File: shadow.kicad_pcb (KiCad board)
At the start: 2 copper layers, 25 parts, among them IC1 FS312F-G, J1 USB_C_Receptacle, Q1 FS8205, SW1 SW_Push, SW2 SW_Push, SW3 SW_SPST, U1 Arduino Nano 33 IoT, U8 TP4056, U9 MT3608

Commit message: start work on pcb design
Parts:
- added C5: 10uf, Capacitor_SMD:C_0201_0603Metric, B.Cu at (70.2, 77.0)
- added C6: 10uf, Capacitor_SMD:C_0201_0603Metric, B.Cu at (72.1, 109.0)
- added GPIO_L1: Conn_01x15, Connector_PinSocket_2.54mm:PinSocket_1x15_P2.54mm_Vertical, F.Cu at (102.9, 122.0)
- added GPIO_R1: Conn_01x15, Connector_PinSocket_2.54mm:PinSocket_1x15_P2.54mm_Vertical, F.Cu at (137.2, 86.4)
- added I2C_PINOUT0: Conn_01x04, Connector_PinSocket_2.54mm:PinSocket_1x04_P2.54mm_Vertical, F.Cu at (170.2, 105.4)
- added I2C_PINOUT1: Conn_01x04, Connector_PinSocket_2.54mm:PinSocket_1x04_P2.54mm_Vertical, F.Cu at (175.3, 105.4)
- added I2C_PINOUT10: Conn_01x04, Connector_PinSocket_2.54mm:PinSocket_1x04_P2.54mm_Vertical, F.Cu at (177.8, 85.1)
- added I2C_PINOUT11: Conn_01x04, Connector_PinSocket_2.54mm:PinSocket_1x04_P2.54mm_Vertical, F.Cu at (177.8, 80.0)
- added I2C_PINOUT12: Conn_01x04, Connector_PinSocket_2.54mm:PinSocket_1x04_P2.54mm_Vertical, F.Cu at (177.8, 74.9)
- added I2C_PINOUT2: Conn_01x04, Connector_PinSocket_2.54mm:PinSocket_1x04_P2.54mm_Vertical, F.Cu at (180.3, 105.4)
- added I2C_PINOUT3: Conn_01x04, Connector_PinSocket_2.54mm:PinSocket_1x04_P2.54mm_Vertical, F.Cu at (185.4, 105.4)
- added I2C_PINOUT4: Conn_01x04, Connector_PinSocket_2.54mm:PinSocket_1x04_P2.54mm_Vertical, F.Cu at (170.2, 120.7)
- added I2C_PINOUT5: Conn_01x04, Connector_PinSocket_2.54mm:PinSocket_1x04_P2.54mm_Vertical, F.Cu at (175.3, 120.7)
- added I2C_PINOUT6: Conn_01x04, Connector_PinSocket_2.54mm:PinSocket_1x04_P2.54mm_Vertical, F.Cu at (180.3, 120.7)
- added I2C_PINOUT7: Conn_01x04, Connector_PinSocket_2.54mm:PinSocket_1x04_P2.54mm_Vertical, F.Cu at (185.4, 120.7)
- added I2C_PINOUT8: Conn_01x04, Connector_PinSocket_2.54mm:PinSocket_1x04_P2.54mm_Vertical, F.Cu at (177.8, 95.2)
- added I2C_PINOUT9: Conn_01x04, Connector_PinSocket_2.54mm:PinSocket_1x04_P2.54mm_Vertical, F.Cu at (177.8, 90.2)
- added JP1: SolderJumper_2_Open, Jumper:SolderJumper-2_P1.3mm_Open_Pad1.0x1.5mm, B.Cu at (64.1, 75.1)
- added JP10: SolderJumper_2_Open, Jumper:SolderJumper-2_P1.3mm_Open_Pad1.0x1.5mm, B.Cu at (66.7, 121.4)
- added JP2: SolderJumper_2_Open, Jumper:SolderJumper-2_P1.3mm_Open_Pad1.0x1.5mm, B.Cu at (64.1, 78.7)
- added JP3: SolderJumper_2_Open, Jumper:SolderJumper-2_P1.3mm_Open_Pad1.0x1.5mm, B.Cu at (64.1, 82.2)
- added JP4: SolderJumper_2_Open, Jumper:SolderJumper-2_P1.3mm_Open_Pad1.0x1.5mm, B.Cu at (64.1, 85.8)
- added JP5: SolderJumper_2_Open, Jumper:SolderJumper-2_P1.3mm_Open_Pad1.0x1.5mm, B.Cu at (64.1, 89.3)
- added JP6: SolderJumper_2_Open, Jumper:SolderJumper-2_P1.3mm_Open_Pad1.0x1.5mm, B.Cu at (66.7, 107.2)
- added JP7: SolderJumper_2_Open, Jumper:SolderJumper-2_P1.3mm_Open_Pad1.0x1.5mm, B.Cu at (66.7, 110.8)
- added JP8: SolderJumper_2_Open, Jumper:SolderJumper-2_P1.3mm_Open_Pad1.0x1.5mm, B.Cu at (66.7, 114.3)
- added JP9: SolderJumper_2_Open, Jumper:SolderJumper-2_P1.3mm_Open_Pad1.0x1.5mm, B.Cu at (66.7, 117.8)
- added MOTOR_CONN1: Conn_01x02, Connector_PinSocket_2.54mm:PinSocket_1x02_P2.54mm_Vertical, F.Cu at (120.7, 147.3)
- added OLED_CONN1: Conn_01x04, Connector_PinSocket_2.54mm:PinSocket_1x04_P2.54mm_Vertical, F.Cu at (100.3, 133.3)
- added PICO_L1: Conn_01x15, Connector_PinSocket_2.54mm:PinSocket_1x15_P2.54mm_Vertical, F.Cu at (110.5, 86.4)
- added PICO_R1: Conn_01x15, Connector_PinSocket_2.54mm:PinSocket_1x15_P2.54mm_Vertical, F.Cu at (129.5, 86.4)
- added R10: 10k, Resistor_SMD:R_0201_0603Metric, B.Cu at (70.2, 80.5)
- added R11: 10k, Resistor_SMD:R_0201_0603Metric, B.Cu at (70.2, 82.2)
- added R12: 10k, Resistor_SMD:R_0201_0603Metric, B.Cu at (70.2, 84.0)
- added R13: 10k, Resistor_SMD:R_0201_0603Metric, B.Cu at (70.2, 85.7)
- added R14: 10k, Resistor_SMD:R_0201_0603Metric, B.Cu at (70.2, 87.5)
- added R15: 10k, Resistor_SMD:R_0201_0603Metric, B.Cu at (72.1, 110.8)
- added R16: 10k, Resistor_SMD:R_0201_0603Metric, B.Cu at (72.1, 112.5)
- added R17: 10k, Resistor_SMD:R_0201_0603Metric, B.Cu at (72.1, 114.3)
- added R18: 10k, Resistor_SMD:R_0201_0603Metric, B.Cu at (72.1, 116.0)
- added R19: 10k, Resistor_SMD:R_0201_0603Metric, B.Cu at (72.1, 117.8)
- added R20: 10k, Resistor_SMD:R_0201_0603Metric, B.Cu at (72.1, 119.5)
- added R9: 10k, Resistor_SMD:R_0201_0603Metric, B.Cu at (70.2, 78.7)
- added RST_SW1: SW_Push, Button_Switch_THT:SW_PUSH_6mm, F.Cu at (130.7, 143.8)
- added SENSOR_CONN1: Conn_01x04, Connector_PinSocket_2.54mm:PinSocket_1x04_P2.54mm_Vertical, B.Cu at (118.1, 73.7)
- added U2: TCA9548APWR, Package_SO:TSSOP-24_4.4x7.8mm_P0.65mm, F.Cu at (195.6, 115.6)
- added UART1: Conn_01x03, Connector_PinSocket_2.54mm:PinSocket_1x03_P2.54mm_Vertical, F.Cu at (94.0, 147.3)
- added US_SENSOR_CONN1: Conn_01x04, Connector_PinSocket_2.54mm:PinSocket_1x04_P2.54mm_Vertical, F.Cu at (123.2, 73.6)
- C3, C4, D4, R1, R2, R3, R4, R5, R6, R7, R8: moved to B.Cu
- SW1, SW2: footprint Button_Switch_THT:SW_PUSH-12mm -> Button_Switch_THT:SW_PUSH_6mm
- U1: value Arduino Nano 33 IoT -> TCA9548APWR; footprint Arduino Nano 33 IoT:MODULE_ABX00027 -> Package_SO:TSSOP-24_4.4x7.8mm_P0.65mm
- moved U1 115.1 mm to (195.6, 85.1)
- moved SW1 80.6 mm to (124.3, 133.3)
- moved SW2 78.3 mm to (137.2, 133.3)
- moved Q1 70.6 mm to (73.7, 83.2)
- moved D4 63.1 mm to (182.1, 112.7), turned to 180 degrees
- moved L1 57.1 mm to (88.9, 99.5), turned to 90 degrees
- moved C1 55.6 mm to (96.0, 102.9)
- moved U9 55.1 mm to (96.5, 82.5)
- moved C3 54.4 mm to (184.1, 84.5), turned to 180 degrees
- moved C4 54.4 mm to (184.1, 86.2), turned to 180 degrees
- moved R1 54.4 mm to (184.1, 88.0), turned to 180 degrees
- moved R2 54.4 mm to (184.1, 89.8), turned to 180 degrees
- moved R3 54.4 mm to (184.1, 91.5), turned to 180 degrees
- moved R4 50.5 mm to (181.7, 84.5), turned to 180 degrees
- moved R5 50.5 mm to (181.7, 86.2), turned to 180 degrees
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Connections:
- C2 pad 2: S1_VCC -> VCC
- D4 pad 1: S1_VCC -> VCC
- R2 pad 1: S1_VCC -> VCC
- SW1 pad 1: Net-(U1-D2) -> /GPIO23
- SW2 pad 1: Net-(U1-D3/PWM) -> /GPIO24
- U1 pad 1: SDA -> Net-(JP5-B)
- U1 pad 10: S7_OUT -> /I2C_PINOUT8/SDA
- U1 pad 11: unconnected-(U1-A7-Pad11) -> /I2C_PINOUT8/SCL
- U1 pad 12: unconnected-(U1-VUSB-Pad12) -> GND
- U1 pad 13: unconnected-(U1-~{RESET}-Pad13) -> /I2C_PINOUT9/SDA
- U1 pad 14: GND -> /I2C_PINOUT9/SCL
- U1 pad 15: S1_VCC -> /I2C_PINOUT10/SDA
- U1 pad 16: unconnected-(U1-TX-Pad16) -> /I2C_PINOUT10/SCL
- U1 pad 17: unconnected-(U1-RX-Pad17) -> /I2C_PINOUT11/SDA
- U1 pad 18: unconnected-(U1-~{RESET}-Pad18) -> /I2C_PINOUT11/SCL
- U1 pad 19: GND -> /I2C_PINOUT12/SDA
- U1 pad 2: unconnected-(U1-+3V3-Pad2) -> Net-(JP4-B)
- U1 pad 20: Net-(U1-D2) -> /I2C_PINOUT12/SCL
- U1 pad 21: Net-(U1-D3/PWM) -> Net-(JP3-A)
- U1 pad 22: unconnected-(U1-D4-Pad22) -> /GPIO6
- U1 pad 23: unconnected-(U1-D5/PWM-Pad23) -> /GPIO5
- U1 pad 24: unconnected-(U1-D6/PWM-Pad24) -> VCC
- U1 pad 3: unconnected-(U1-AREF-Pad3) -> Net-(U1-~{RESET})
- U1 pad 4: S1_OUT -> /SENSOR_SDA
- U1 pad 5: S2_OUT -> /SENSOR_SCL
- U1 pad 6: S3_OUT -> /US_SDA
- U1 pad 7: S4_OUT -> /US_SCL
- U1 pad 8: S5_OUT -> /OLED_SDA
- U1 pad 9: S6_OUT -> /OLED_SCL
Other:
- board outline added: 69.8 x 86.4 mm
- board text added: "OLED TODO: move"

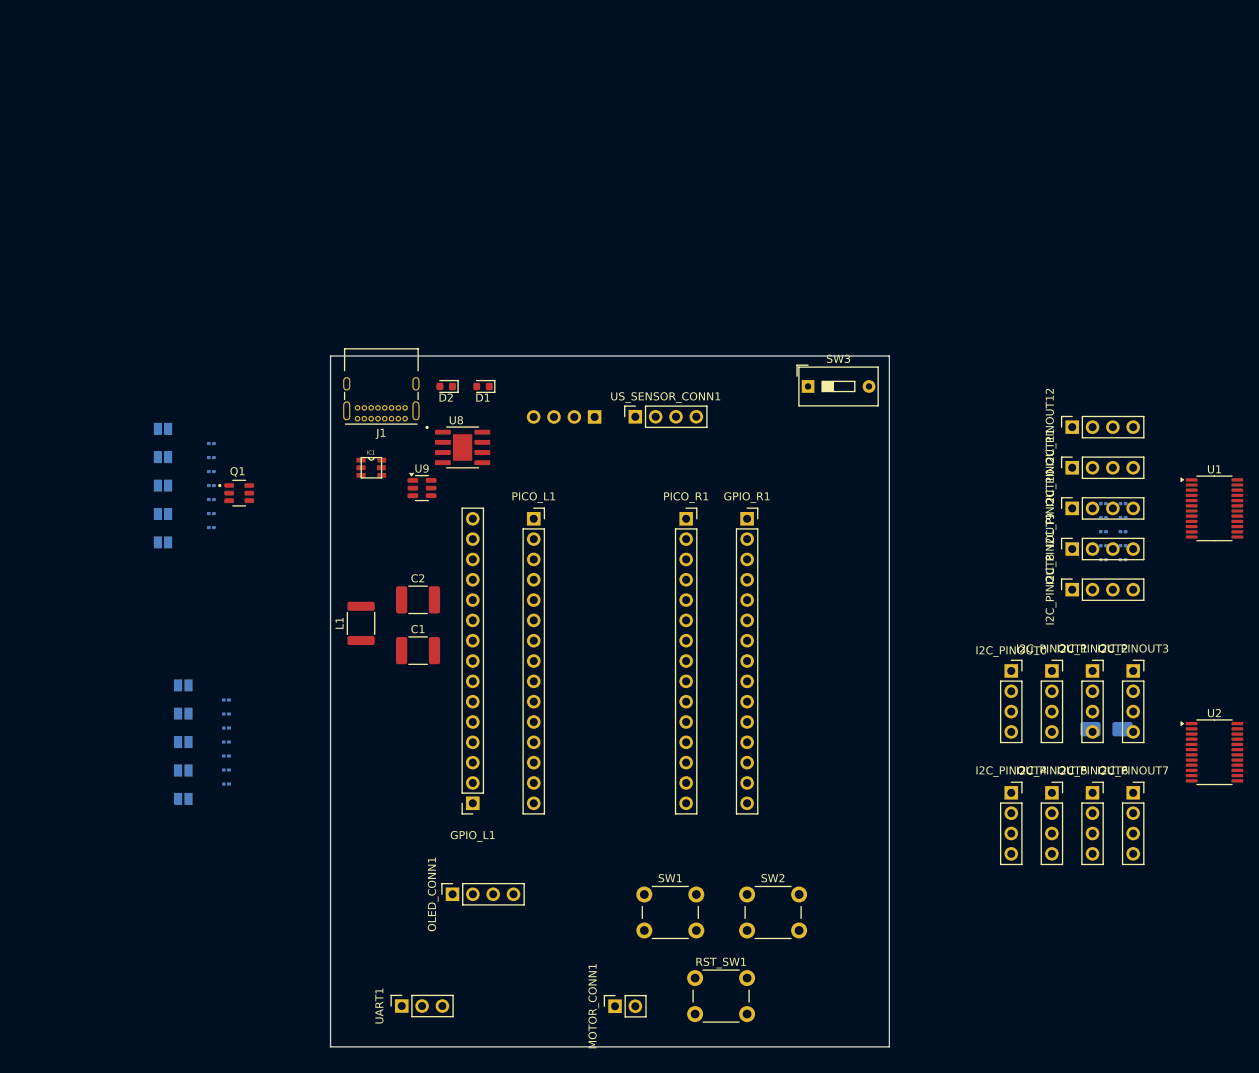
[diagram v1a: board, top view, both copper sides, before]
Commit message: Add new lipo charger to pcb
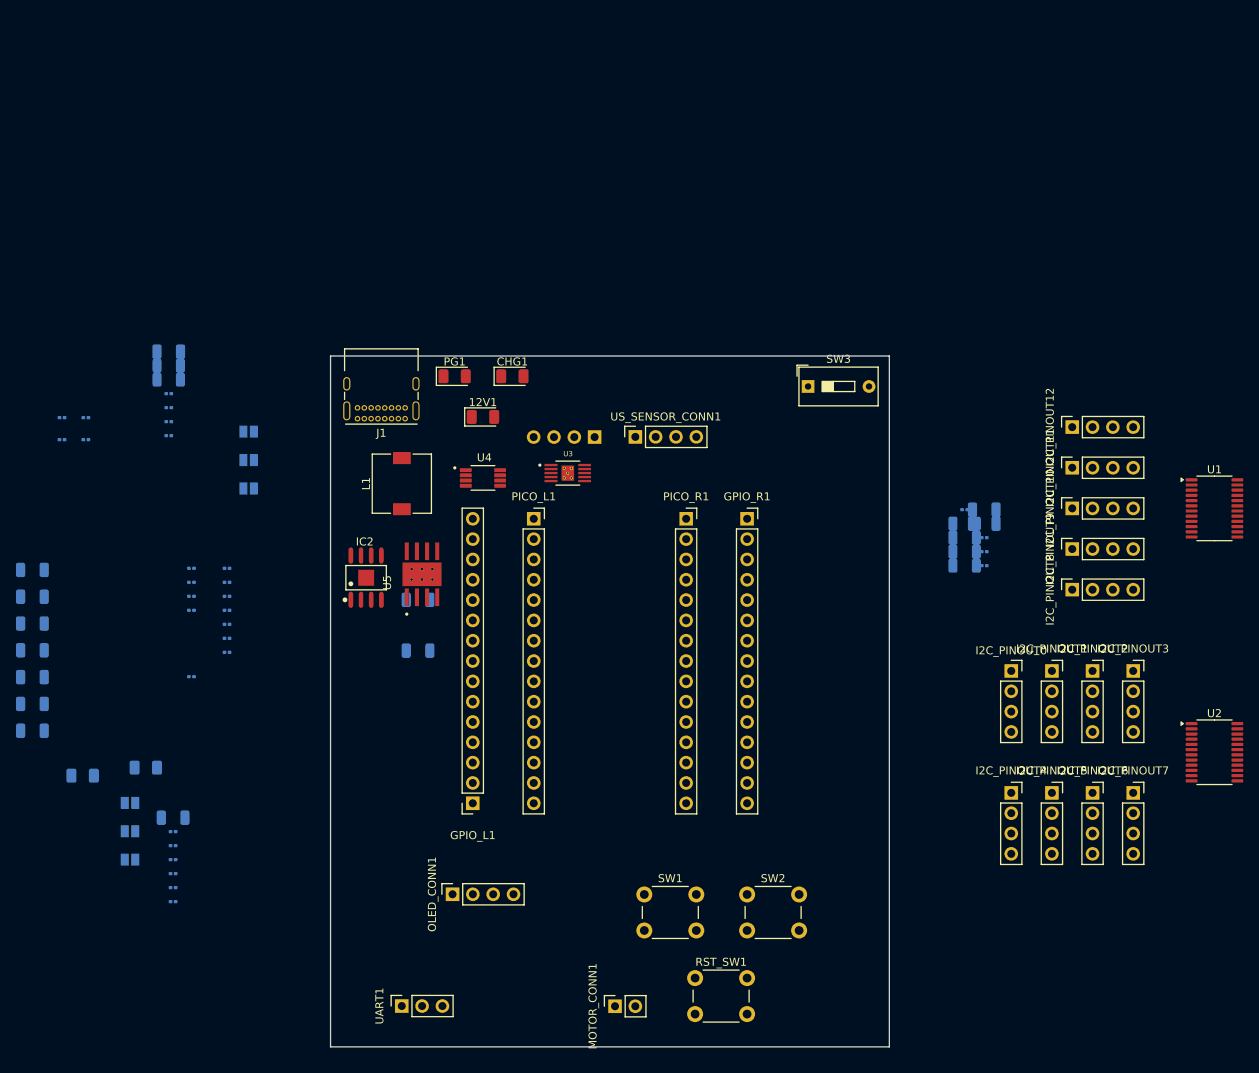
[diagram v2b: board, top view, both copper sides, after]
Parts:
- removed D4: SS34, Diode_SMD:D_SMA
- removed IC1: FS312F-G, FS312F-G:SOT23-6
- removed JP1, JP10, JP2, JP9: SolderJumper_2_Open, Jumper:SolderJumper-2_P1.3mm_Open_Pad1.0x1.5mm
- removed Q1: FS8205, FS8205:SOT95P280X145-6N
- removed U8: TP4056, TP4056:SOP127P600X175-9N
- removed U9: MT3608, Package_TO_SOT_SMD:SOT-23-6
- added 12V1: LED_R, LED_SMD:LED_1206_3216Metric, F.Cu at (104.1, 73.7)
- added C10: 10nF, Capacitor_SMD:C_1206_3216Metric, B.Cu at (47.8, 102.8)
- added C11: 100nF, Capacitor_SMD:C_1206_3216Metric, B.Cu at (47.8, 106.2)
- added C12: 470nF, Capacitor_SMD:C_1206_3216Metric, B.Cu at (47.8, 109.5)
- added C13: 330u/35V, Capacitor_SMD:C_1206_3216Metric, B.Cu at (47.8, 112.9)
- added C14: 10uf, Capacitor_SMD:C_0201_0603Metric, B.Cu at (67.7, 92.6)
- added C15: 10uf, Capacitor_SMD:C_0201_0603Metric, B.Cu at (72.2, 92.6)
- added C7: 100nF, Capacitor_SMD:C_1206_3216Metric, B.Cu at (47.8, 92.8)
- added C8: 10uF, Capacitor_SMD:C_1206_3216Metric, B.Cu at (47.8, 96.1)
- added C9: 10uF, Capacitor_SMD:C_1206_3216Metric, B.Cu at (47.8, 99.5)
- added CHG1: LED_R, LED_SMD:LED_1206_3216Metric, F.Cu at (107.8, 68.6)
- added IC2: XB8089D, XB8089D:XB8089D, F.Cu at (89.5, 93.8)
- added PG1: LED_G, LED_SMD:LED_1206_3216Metric, F.Cu at (100.6, 68.6)
- added R21: 10k, Resistor_SMD:R_0201_0603Metric, B.Cu at (67.7, 94.3)
- added R22: 10k, Resistor_SMD:R_0201_0603Metric, B.Cu at (67.7, 96.1)
- added R23: 10k, Resistor_SMD:R_0201_0603Metric, B.Cu at (67.7, 97.8)
- added R24: 10k, Resistor_SMD:R_0201_0603Metric, B.Cu at (72.2, 94.3)
- added R25: 10k, Resistor_SMD:R_0201_0603Metric, B.Cu at (72.2, 96.1)
- added R26: 10k, Resistor_SMD:R_0201_0603Metric, B.Cu at (72.2, 97.8)
- added R27: 10k, Resistor_SMD:R_0201_0603Metric, B.Cu at (72.2, 99.6)
- added R28: 10k, Resistor_SMD:R_0201_0603Metric, B.Cu at (72.2, 101.3)
- added R29: 10k, Resistor_SMD:R_0201_0603Metric, B.Cu at (72.2, 103.1)
- added R30: 0k, Resistor_SMD:R_0201_0603Metric, B.Cu at (67.7, 106.1)
- added R31: 0k, Resistor_SMD:R_0201_0603Metric, B.Cu at (54.5, 73.8)
- added R32: 0k, Resistor_SMD:R_0201_0603Metric, B.Cu at (51.5, 73.8)
- added R33: 0k, Resistor_SMD:R_0201_0603Metric, B.Cu at (54.5, 76.5)
- added R34: 0k, Resistor_SMD:R_0201_0603Metric, B.Cu at (51.5, 76.5)
- added U3: BQ24092DGQR, BQ24092DGQR:IC_XTR111AIDGQR, F.Cu at (114.8, 80.7)
- added U4: TPS61085DGKR, TPS61085DGKR:SOP65P490X110-8N, F.Cu at (104.1, 81.3)
- added U5: TPS259621DDAT, TPS259621:IC_TPS259621DDAT, F.Cu at (96.5, 93.3)
- C1: value 22uF -> 3.3nF; footprint Capacitor_SMD:C_1812_4532Metric -> Capacitor_SMD:C_1206_3216Metric; moved to B.Cu
- C2: value 22uF -> 100n; footprint Capacitor_SMD:C_1812_4532Metric -> Capacitor_SMD:C_1206_3216Metric; moved to B.Cu
- C3: value 10u -> 10uF; footprint Capacitor_SMD:C_0201_0603Metric -> Capacitor_SMD:C_1206_3216Metric
- C4: value 0.1u -> 10uF; footprint Capacitor_SMD:C_0201_0603Metric -> Capacitor_SMD:C_1206_3216Metric
- C5: value 10uf -> 1uF; footprint Capacitor_SMD:C_0201_0603Metric -> Capacitor_SMD:C_1206_3216Metric
- C6: value 10uf -> 10uF; footprint Capacitor_SMD:C_0201_0603Metric -> Capacitor_SMD:C_1206_3216Metric
- D1: value LEDG -> D_Schottky; footprint LED_SMD:LED_0603_1608Metric -> Diode_SMD:D_1206_3216Metric; moved to B.Cu
- D2: value LEDR -> D_Schottky; footprint LED_SMD:LED_0603_1608Metric -> Diode_SMD:D_1206_3216Metric; moved to B.Cu
- L1: value 22uH -> 3.3u; footprint Inductor_SMD:L_1812_4532Metric -> Inductor_SMD:L_7.3x7.3_H4.5
- R1: value 1k -> 84.5k
- R10: footprint Resistor_SMD:R_0201_0603Metric -> Resistor_SMD:R_1206_3216Metric
- R11: value 10k -> 100k
- R12, R13: value 10k -> 1.2k
- R14: value 10k -> 4.7k
- R15: value 10k -> 1.8k
- R16, R17: value 10k -> 0k
- R2: value 7.5k -> 158k
- R3: value 1k -> 18k
- R4: value 1k -> 13k
- R5, R7: value 2k -> 1k; footprint Resistor_SMD:R_0201_0603Metric -> Resistor_SMD:R_1206_3216Metric
- R6: value 100 -> 536; footprint Resistor_SMD:R_0201_0603Metric -> Resistor_SMD:R_1206_3216Metric
- R8: value 0k -> 1.5k; footprint Resistor_SMD:R_0201_0603Metric -> Resistor_SMD:R_1206_3216Metric
- R9: value 10k -> 1.5k; footprint Resistor_SMD:R_0201_0603Metric -> Resistor_SMD:R_1206_3216Metric
- moved D1 69.8 mm to (54.1, 118.5), turned to 0 degrees
- moved D2 60.7 mm to (62.0, 117.5), turned to 0 degrees
- moved L1 18.2 mm to (94.0, 82.0)
- moved C3 17.4 mm to (166.8, 85.2)
- moved C4 17.4 mm to (166.8, 87.0)
- moved R1 17.4 mm to (166.8, 88.8)
- moved R2 17.4 mm to (166.8, 90.5)
- moved R3 17.4 mm to (166.8, 92.2)
- moved R4 17.4 mm to (164.4, 85.2)
- moved R5 17.4 mm to (164.4, 87.0)
- moved R6 17.4 mm to (164.4, 88.8)
- moved R7 17.4 mm to (164.4, 90.5)
- moved R8 17.4 mm to (164.4, 92.2)
- moved C6 16.1 mm to (65.4, 123.8)
- moved R15 16.1 mm to (65.4, 125.5)
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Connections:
- C1 pad 1: GND -> Net-(C1-Pad1)
- C1 pad 2: Net-(SW3-B) -> GND
- C2 pad 1: GND -> Net-(U4-SS)
- C2 pad 2: VCC -> GND
- C3 pad 1: Net-(U8-CE) -> Net-(D1-K)
- C4 pad 1: BAT- -> Net-(D1-K)
- C4 pad 2: Net-(IC1-VCC) -> GND
- C5 pad 1: VCC -> Net-(SW3-B)
- C6 pad 1: VCC -> Net-(SW3-B)
- D2 pad 1: Net-(D2-K) -> GND
- D2 pad 2: Net-(D1-A) -> GND
- GPIO_R1 pad 14: VCC -> GND
- I2C_PINOUT0 pad 3: VCC -> GND
- I2C_PINOUT1 pad 3: VCC -> GND
- I2C_PINOUT10 pad 3: VCC -> GND
- I2C_PINOUT11 pad 3: VCC -> GND
- I2C_PINOUT12 pad 3: VCC -> GND
- I2C_PINOUT2 pad 3: VCC -> GND
- I2C_PINOUT3 pad 3: VCC -> GND
- I2C_PINOUT4 pad 3: VCC -> GND
- I2C_PINOUT5 pad 3: VCC -> GND
- I2C_PINOUT6 pad 3: VCC -> GND
- I2C_PINOUT7 pad 3: VCC -> GND
- I2C_PINOUT8 pad 3: VCC -> GND
- I2C_PINOUT9 pad 3: VCC -> GND
- J1 pad A4: Net-(U8-CE) -> GND
- J1 pad A9: Net-(U8-CE) -> GND
- J1 pad B4: Net-(U8-CE) -> GND
- J1 pad B9: Net-(U8-CE) -> GND
- JP3 pad 2: VCC -> GND
- JP4 pad 1: VCC -> GND
- JP5 pad 1: VCC -> GND
- JP6 pad 2: VCC -> GND
- JP7 pad 1: VCC -> GND
- JP8 pad 1: VCC -> GND
- L1 pad 2: Net-(D4-A) -> Net-(D1-A)
- OLED_CONN1 pad 1: VCC -> GND
- PICO_R1 pad 14: VCC -> GND
- R1 pad 1: Net-(U8-~{STDBY}) -> Net-(U4-FB)
- R1 pad 2: Net-(D1-K) -> Net-(R1-Pad2)
- R10 pad 1: VCC -> GND
- R11 pad 1: VCC -> GND
- R11 pad 2: Net-(U1-~{RESET}) -> Net-(U5-EN/UVLO)
- R12 pad 2: Net-(JP3-A) -> Net-(U5-ILM)
- R13 pad 2: Net-(JP4-B) -> Net-(R13-Pad2)
- R14 pad 1: GND -> Net-(12V1-A)
- R14 pad 2: Net-(JP5-B) -> GND
- R15 pad 2: Net-(JP6-A) -> Net-(12V1-A)
- R16 pad 1: GND -> Net-(R1-Pad2)
- R16 pad 2: Net-(JP7-B) -> Net-(D1-K)
- R17 pad 1: GND -> Net-(R13-Pad2)
- R17 pad 2: Net-(JP8-B) -> Net-(U5-ILM)
- R18 pad 1: VCC -> GND
- R18 pad 2: Net-(U2-~{RESET}) -> Net-(R18-Pad2)
- R19 pad 1: VCC -> GND
- R2 pad 1: VCC -> Net-(U4-FB)
- R2 pad 2: Net-(U9-FB) -> Net-(D1-K)
- R20 pad 1: VCC -> GND
- R20 pad 2: Net-(JP10-B) -> Net-(JP5-B)
- R3 pad 1: Net-(U9-FB) -> GND
- R3 pad 2: GND -> Net-(U4-FB)
- R4 pad 1: Net-(U8-~{CHRG}) -> Net-(C1-Pad1)
- R4 pad 2: Net-(D2-K) -> Net-(U4-COMP)
- R5 pad 2: GND -> BAT+
- R6 pad 1: BAT+ -> Net-(U3-ISET)
- R6 pad 2: Net-(IC1-VCC) -> GND
- R8 pad 1: Net-(J1-SHIELD) -> Net-(PG1-A)
- R8 pad 2: GND -> BAT+
- R9 pad 1: VCC -> Net-(CHG1-A)
- R9 pad 2: Net-(JP2-B) -> BAT+
- SENSOR_CONN1 pad 3: VCC -> GND
- U1 pad 24: VCC -> GND
- U2 pad 24: VCC -> GND
- US_SENSOR_CONN1 pad 3: VCC -> GND

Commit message: a lot of work on pcb
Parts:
- removed SENSOR_CONN1, US_SENSOR_CONN1: Conn_01x04, Connector_PinSocket_2.54mm:PinSocket_1x04_P2.54mm_Vertical
- added ARR1: Conn_01x04, Connector_PinSocket_2.54mm:PinSocket_1x04_P2.54mm_Vertical, B.Cu at (132.1, 68.6)
- added BATT_JST1: JST, Connector_JST:JST_XH_B2B-XH-A_1x02_P2.50mm_Vertical, F.Cu at (133.3, 146.8)
- added US1: Conn_01x04, Connector_PinSocket_2.54mm:PinSocket_1x04_P2.54mm_Vertical, F.Cu at (124.5, 73.7)
- moved I2C_PINOUT12 118.2 mm to (86.4, 149.9), turned to 180 degrees
- moved I2C_PINOUT11 107.8 mm to (86.4, 137.2), turned to 180 degrees
- moved U1 102.3 mm to (96.2, 109.5)
- moved I2C_PINOUT10 99.6 mm to (86.4, 124.5), turned to 180 degrees
- moved I2C_PINOUT9 94.0 mm to (86.4, 111.8), turned to 180 degrees
- moved JP8 91.6 mm to (139.1, 82.8)
- moved I2C_PINOUT8 91.5 mm to (86.4, 99.1), turned to 180 degrees
- moved JP7 91.2 mm to (139.1, 80.0)
- moved R32 90.9 mm to (141.0, 89.8)
- moved JP6 90.8 mm to (139.1, 77.2)
- moved R34 90.1 mm to (141.0, 87.6)
- moved R9 86.3 mm to (143.0, 104.0)
- moved RST_SW1 77.9 mm to (112.2, 68.1)
- moved C7 77.3 mm to (125.1, 92.0), turned to -90 degrees
- moved C3 77.1 mm to (91.4, 69.0)
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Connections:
- net BAT+ renamed /battery/BAT+
- net BAT- renamed /battery/BAT-
- C10 pad 2: GND -> VCC
- C11 pad 2: GND -> VCC
- C12 pad 2: GND -> VCC
- C13 pad 2: GND -> VCC
- C14 pad 1: GND -> VCC
- C15 pad 1: GND -> VCC
- C8 pad 1: GND -> Net-(U3-IN)
- D2 pad 2: GND -> VCC
- GPIO_R1 pad 14: GND -> VCC
- I2C_PINOUT0 pad 3: GND -> VCC
- I2C_PINOUT1 pad 3: GND -> VCC
- I2C_PINOUT10 pad 3: GND -> VCC
- I2C_PINOUT11 pad 3: GND -> VCC
- I2C_PINOUT12 pad 3: GND -> VCC
- I2C_PINOUT2 pad 3: GND -> VCC
- I2C_PINOUT3 pad 3: GND -> VCC
- I2C_PINOUT4 pad 3: GND -> VCC
- I2C_PINOUT5 pad 3: GND -> VCC
- I2C_PINOUT6 pad 3: GND -> VCC
- I2C_PINOUT7 pad 3: GND -> VCC
- I2C_PINOUT8 pad 3: GND -> VCC
- I2C_PINOUT9 pad 3: GND -> VCC
- J1 pad A4: GND -> Net-(U3-IN)
- J1 pad A9: GND -> Net-(U3-IN)
- J1 pad B4: GND -> Net-(U3-IN)
- J1 pad B9: GND -> Net-(U3-IN)
- JP3 pad 2: GND -> VCC
- JP4 pad 1: GND -> VCC
- JP5 pad 1: GND -> VCC
- JP6 pad 2: GND -> VCC
- JP7 pad 1: GND -> VCC
- JP8 pad 1: GND -> VCC
- OLED_CONN1 pad 1: GND -> VCC
- PICO_R1 pad 14: GND -> VCC
- R12 pad 1: GND -> VCC
- R13 pad 1: GND -> VCC
- R18 pad 1: GND -> VCC
- R19 pad 1: GND -> VCC
- R23 pad 1: GND -> VCC
- R26 pad 1: GND -> VCC
- R27 pad 1: GND -> VCC
- R28 pad 1: GND -> VCC
- U1 pad 24: GND -> VCC
- U2 pad 24: GND -> VCC
- U3 pad 1: GND -> Net-(U3-IN)
- U5 pad 1: GND -> VCC
- U5 pad 9: GND -> VCC
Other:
- board text added: "12v"
- board text added: "A0"
- board text added: "A1"
- board text added: "A2"
- board text added: "MPLX1"
- board text added: "MPLX2"

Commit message: finish pcb layout
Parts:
- moved R29 53.1 mm to (143.8, 73.0)
- moved UART1 50.0 mm to (99.1, 127.0), turned to -90 degrees
- moved R25 47.9 mm to (132.4, 81.9)
- moved R24 45.1 mm to (133.0, 75.6)
- moved C7 38.9 mm to (88.3, 79.4), turned to 180 degrees
- moved C2 31.1 mm to (123.8, 81.9)
- moved R1 28.6 mm to (121.3, 97.8), turned to 0 degrees
- moved R3 27.6 mm to (115.9, 95.9)
- moved R2 27.3 mm to (119.4, 95.9), turned to 0 degrees
- moved R16 22.7 mm to (124.8, 96.0), turned to 0 degrees
- moved C1 22.0 mm to (126.4, 77.5)
- moved R5 19.8 mm to (104.8, 79.4), turned to 0 degrees
- moved BATT_JST1 18.5 mm to (150.6, 140.5), turned to 180 degrees
- moved IC2 14.6 mm to (103.5, 80.0)
- moved D1 9.96 mm to (123.8, 92.1)
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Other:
- board size 69.8 x 86.4 mm -> 69.8 x 78.7 mm
